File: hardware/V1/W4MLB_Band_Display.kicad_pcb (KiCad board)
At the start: 2 copper layers, 71 x 64 mm, 27 parts, among them J1 SSW-115-01-G-S, J2 SSW-115-01-G-S, J3 SSQ-108-01-T-D-LL, J4 SAMTEC-TST-108-01-X-D, J5 PJRAN1X1U01X, J6 PJRAN1X1U01X, J7 4DB-P108-02, J8 EJ503B, J9 Conn_01x09, Q1 MMBT2222A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

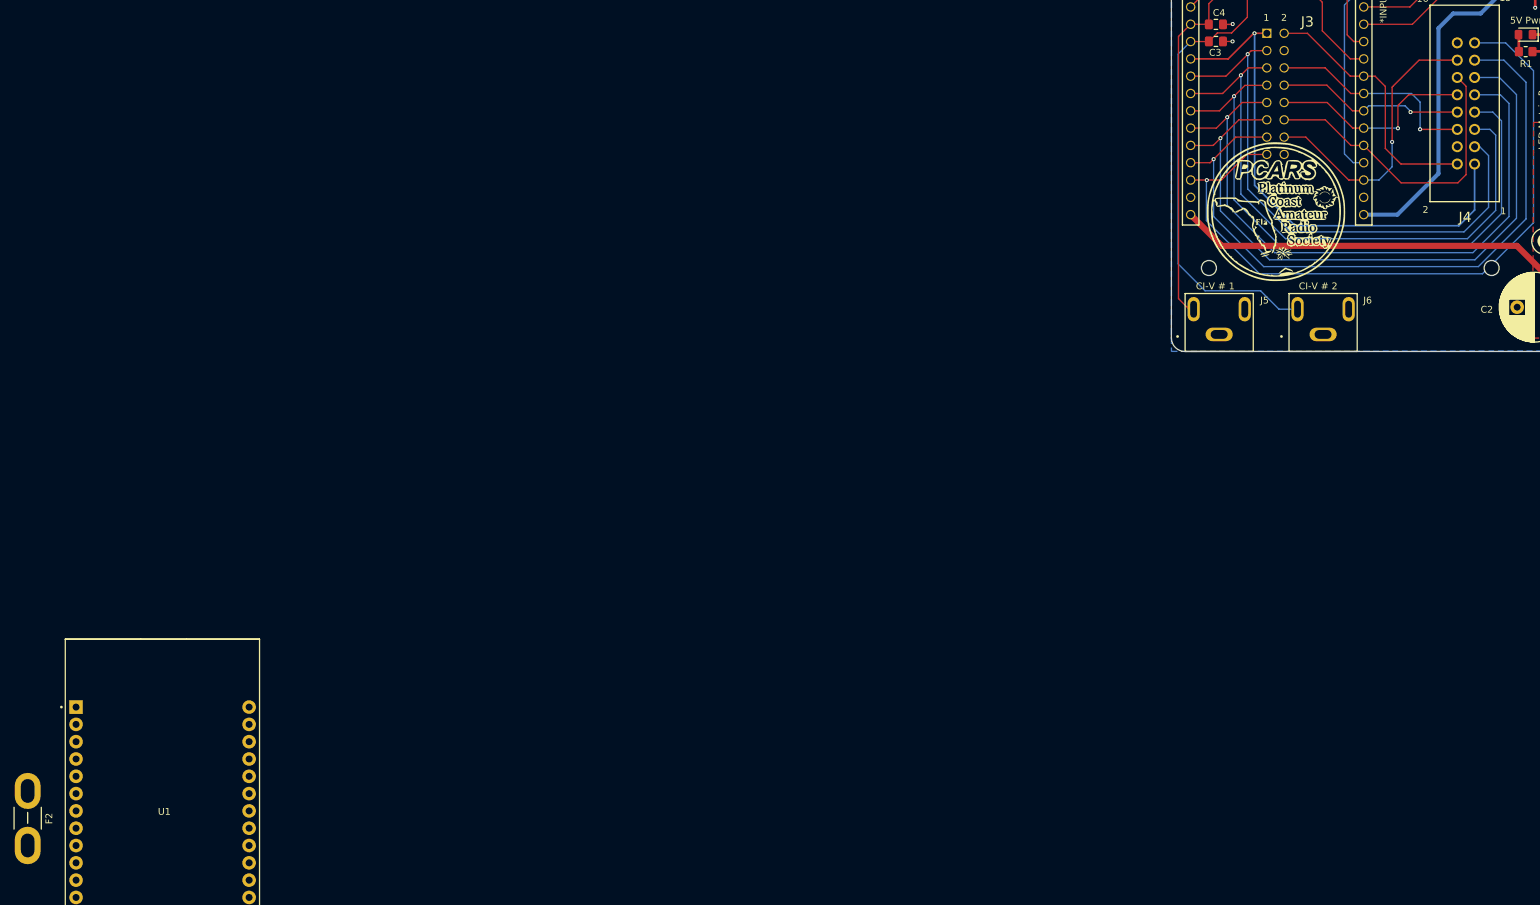
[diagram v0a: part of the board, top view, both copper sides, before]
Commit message: Updates to V1 & V2 boards
Updated location of +5V LED Matric power connector on V2 board after careful measurements.
Made final changes to V1 board before sending off to fabrication.
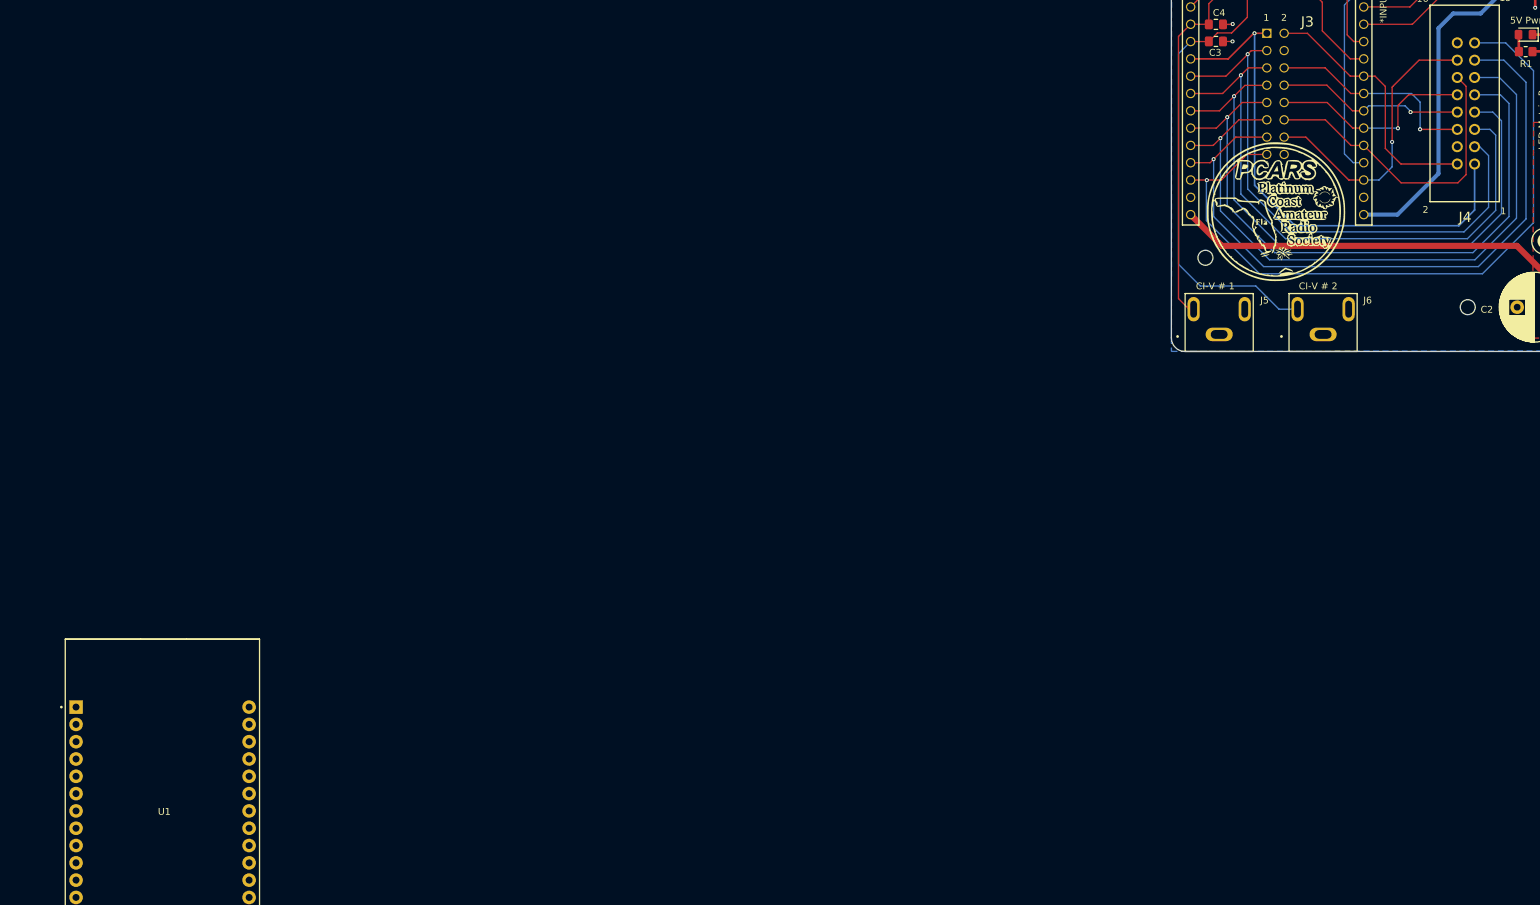
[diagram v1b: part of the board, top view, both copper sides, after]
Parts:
- removed F2: Fuse_Small, Fuse:Fuse_Blade_Mini_directSolder
- moved MH4 6.73 mm to (162.5, 121.0)
- moved MH3 1.58 mm to (124.0, 113.8)

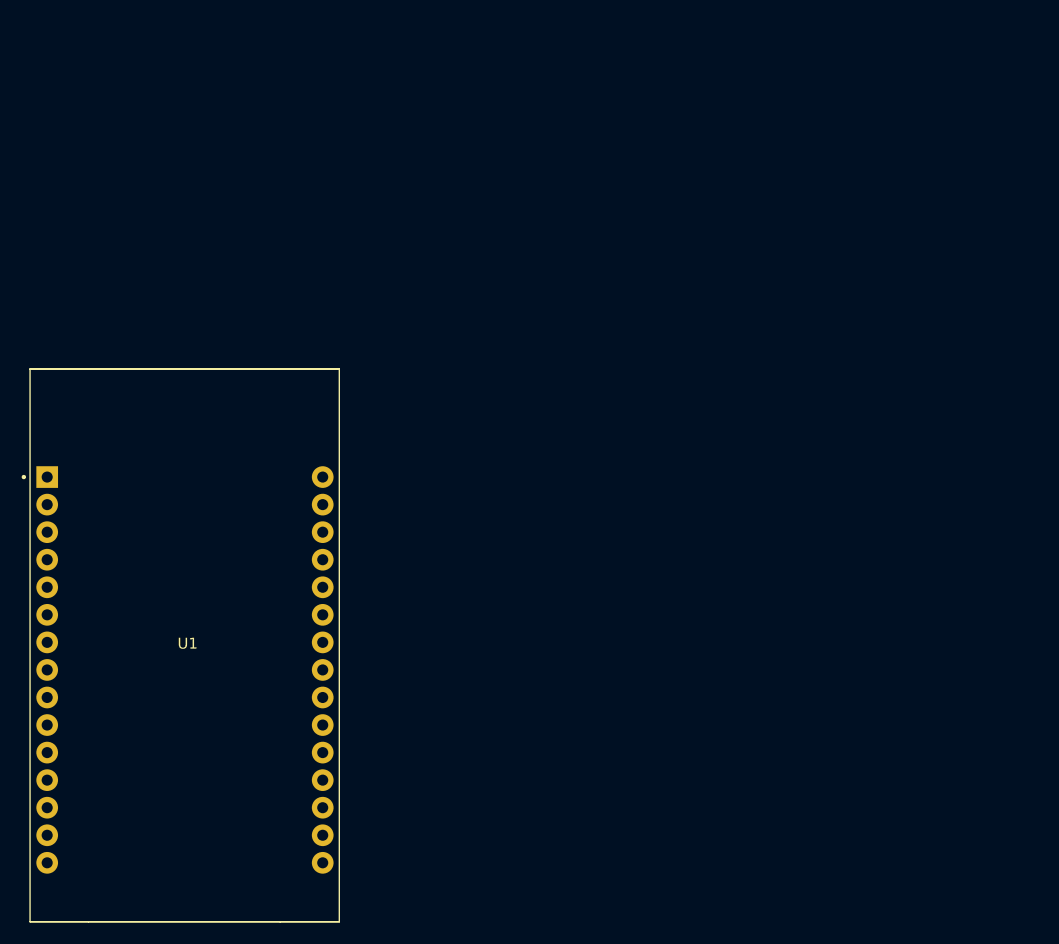
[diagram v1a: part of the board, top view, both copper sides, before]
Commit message: Updated images to reflect actual V1 build
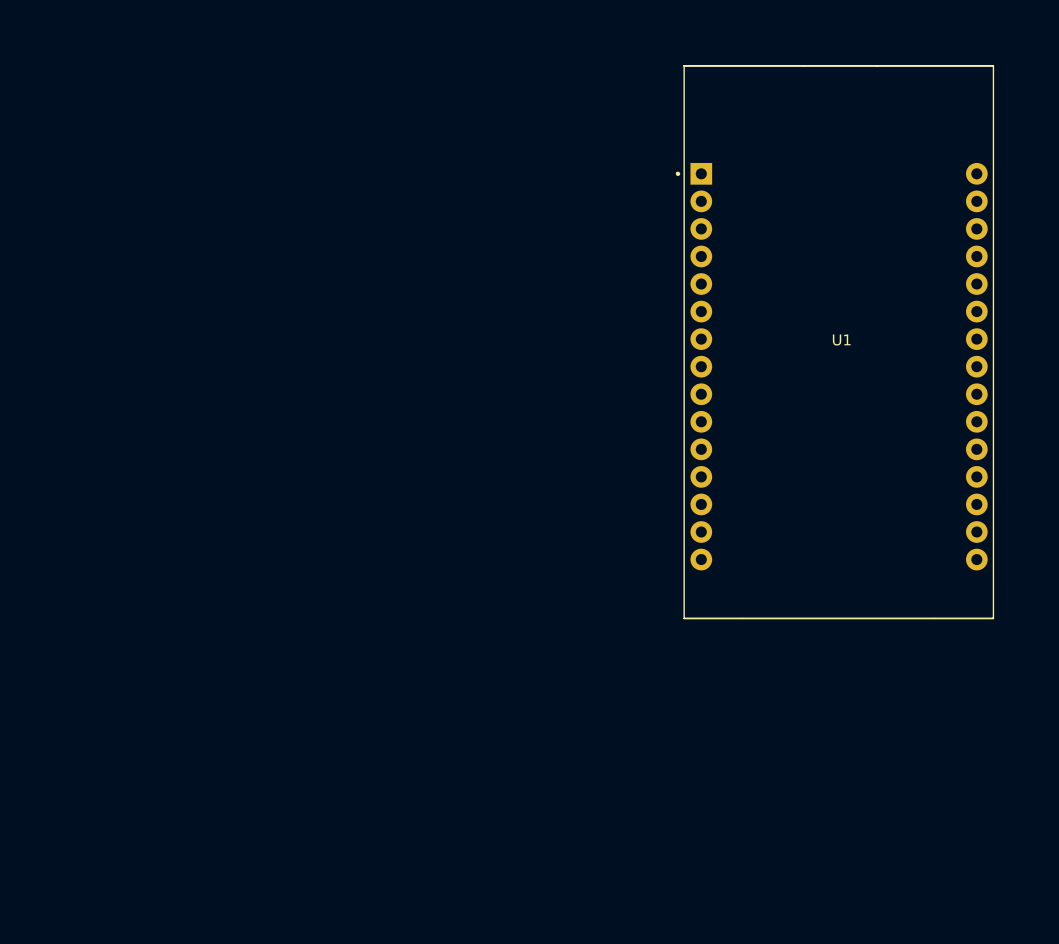
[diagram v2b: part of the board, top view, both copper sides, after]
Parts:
- moved U1 66.5 mm to (31.2, 167.2)
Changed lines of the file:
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@@
 	(footprint "Footprints:MODULE_ESP32_DEVKIT_V1"
 		(layer "F.Cu")
-		(at -29.05 195.205)
+		(at 31.25 167.25)
 		(property "Reference" "U1"
 			(at 0.25 -0.165 0)
@@
 			(polygon
 				(pts
-					(xy -37.96 214.19) (xy -20.27 214.19) (xy -20.27 220.68) (xy -37.96 220.68)
+					(xy 22.34 186.235) (xy 40.03 186.235) (xy 40.03 192.725) (xy 22.34 192.725)
 				)
 			)
@@
 			(polygon
 				(pts
-					(xy -37.96 214.19) (xy -20.27 214.19) (xy -20.27 220.68) (xy -37.96 220.68)
+					(xy 22.34 186.235) (xy 40.03 186.235) (xy 40.03 192.725) (xy 22.34 192.725)
 				)
 			)
@@
 			(polygon
 				(pts
-					(xy -37.96 214.19) (xy -20.27 214.19) (xy -20.27 220.68) (xy -37.96 220.68)
-				)
-			)
+					(xy 22.34 186.235) (xy 40.03 186.235) (xy 40.03 192.725) (xy 22.34 192.725)
+				)
+			)
